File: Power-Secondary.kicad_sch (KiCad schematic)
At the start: 37 parts, among them J1 SUPP PWR MON, J2 SUPP PWR 1, J3 SUPP PWR 2, J4 DCDC SUPPLY, J5 FUSE OUT, J6 SUPP OUT, J7 LV ENABLE, Q1 S1G1D2S2G2D1, Q1A1 IRFU5305PbF, Q1A2 IRFU5305PbF, Q1A3 IRFU5305PbF, Q1A4 IRFU5305PbF, Q2 S1G1D2S2G2D1, Q3 FDD86250-F085

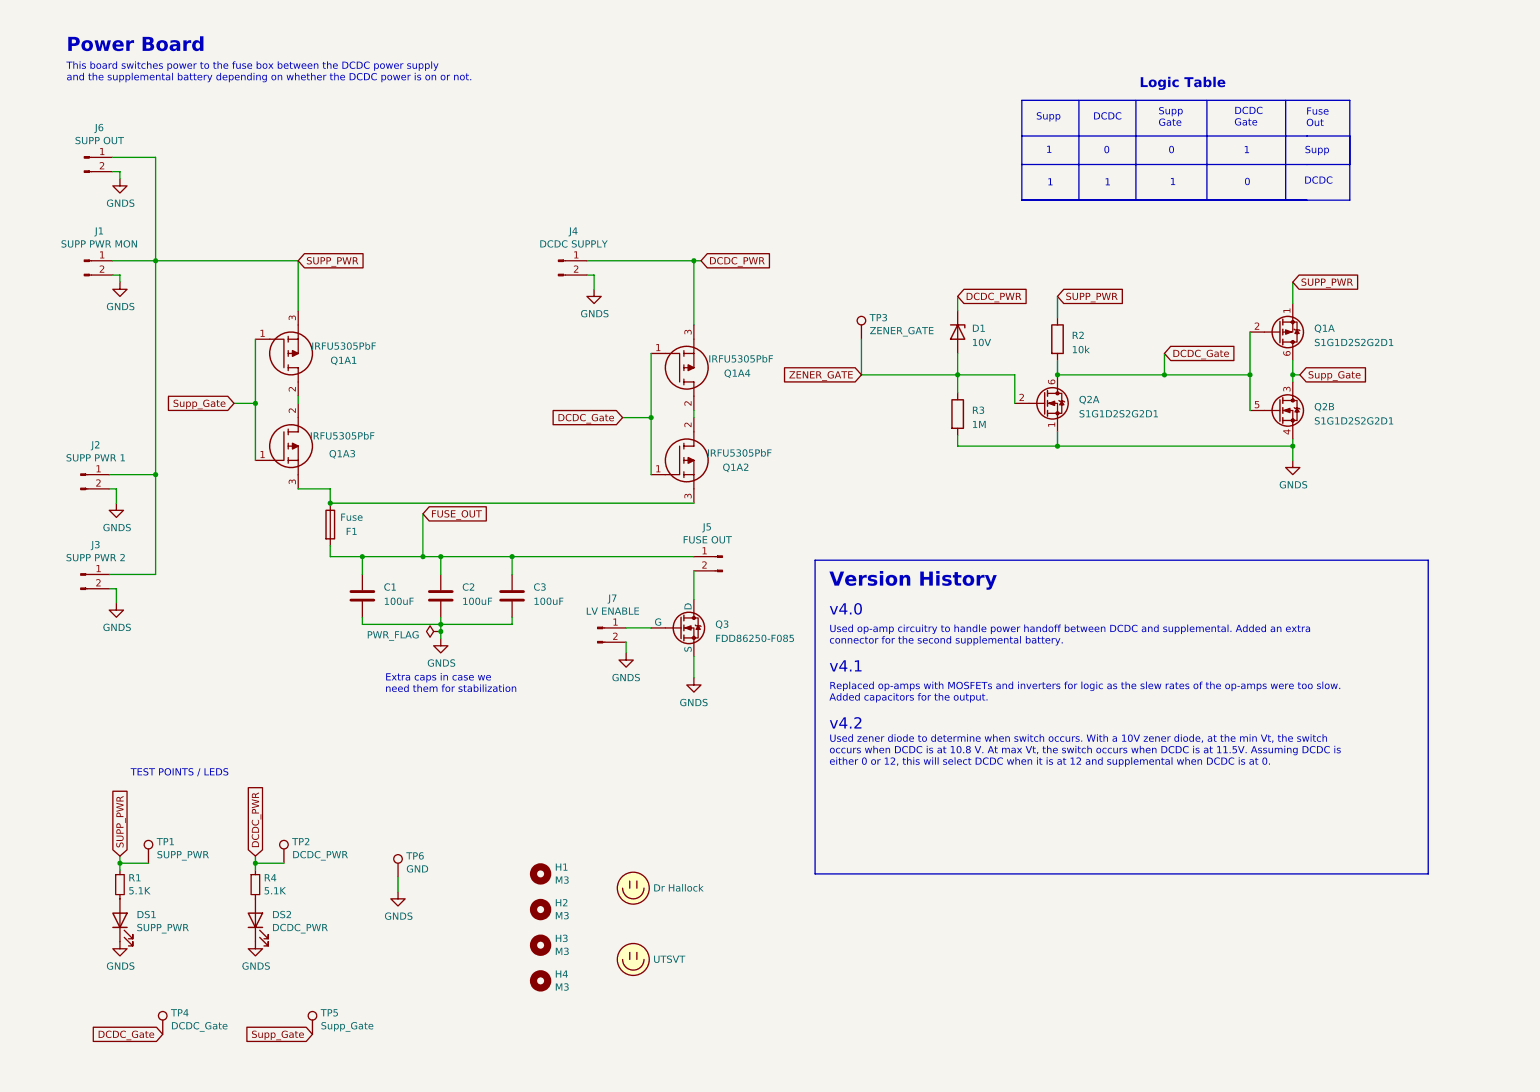
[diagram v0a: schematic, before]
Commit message: Ltc4421 v1.0 (#12)
* LTC4421 Symbol creation

* early sch

* early sch

* changes

* Improved organization of sch

* added circuitry for sch

* Added MOSFET to symbol library

* Finished sch

* footprint assignments

* changes to Power Board sch

* CAD models, symbols update, and footprints

* Pull up and Pull down configs for VALID, DISABLE, SHDN, RETRY

* small changes

* Library fixes and sch changes

* Sch changes

* changes to sch

* assigned footprints

* Excel calculator

* Adjusted resistor divider values and specified more components in the BOM

* Completed BOM for the most part

* sch iteration 1 complete plssssssssss

* final footprint assignments

* initial layout

* added another current sense resistor

* fixed connector pinout

* change SHDN logic

* fixes to sch

* layout complete

* Layout fixes

* made all planes solid filled

* added supp mon connection

* constraint fixes

---------

Co-authored-by: choafe <cryn.hoang@gmail.com>
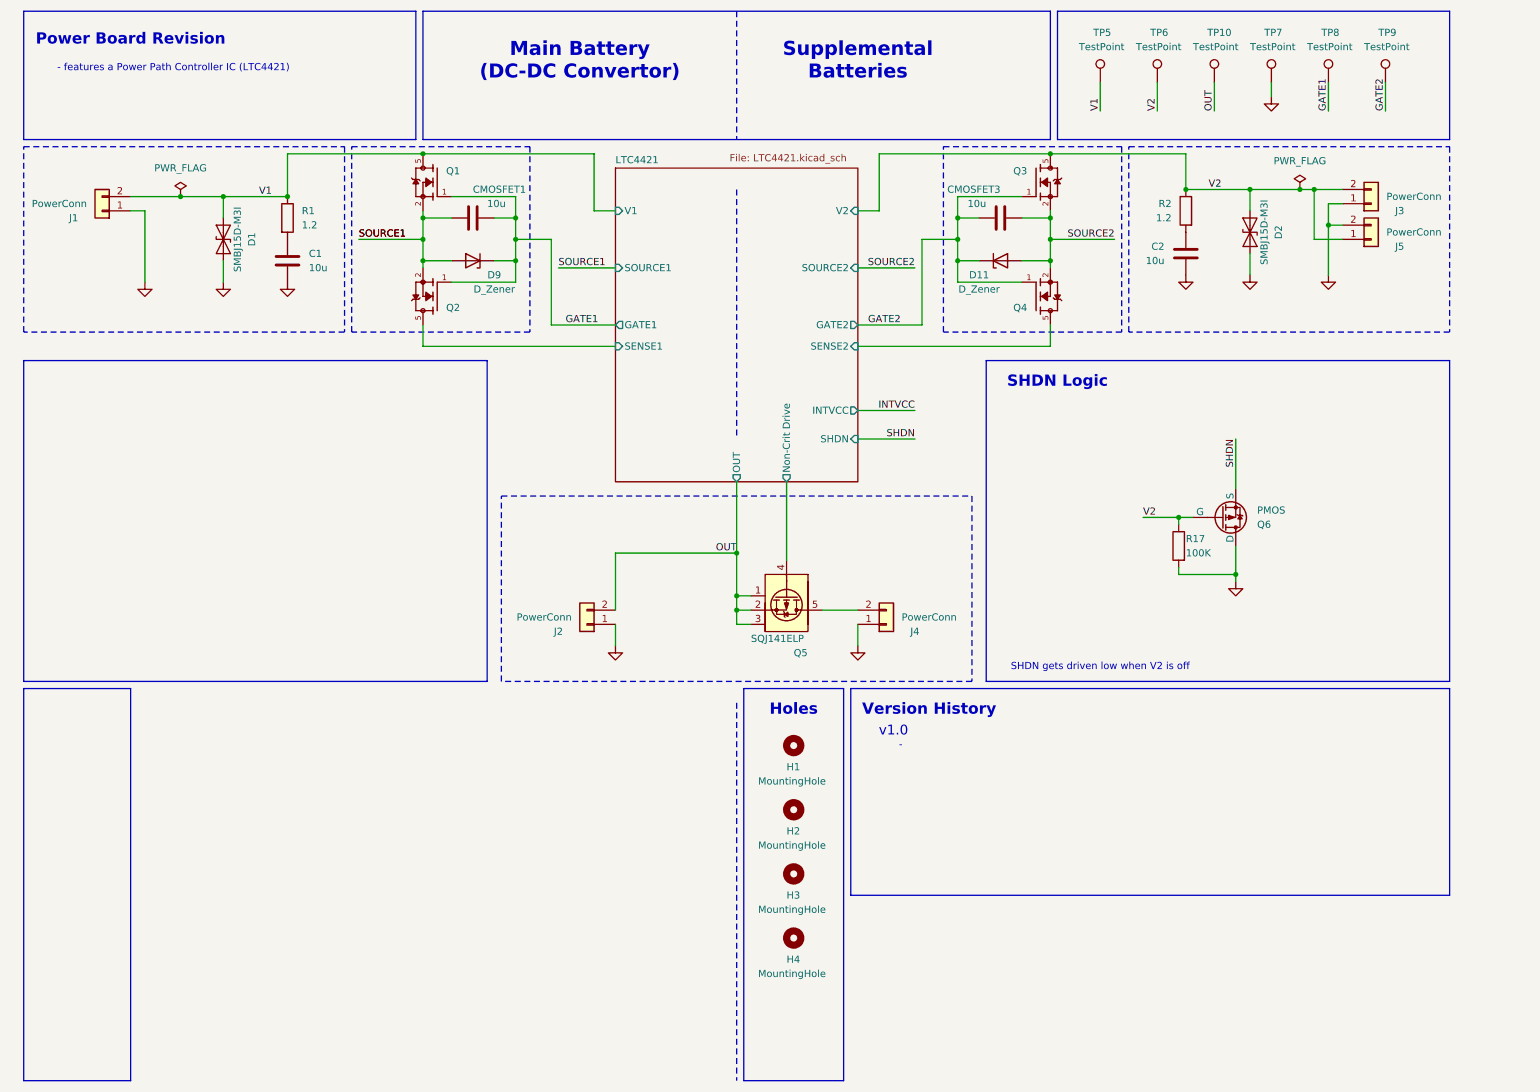
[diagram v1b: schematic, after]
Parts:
- removed C1, C2, C3: 100uF, Capacitor_SMD:C_1210_3225Metric, symbol Device:C
- removed D1: 10V, UTSVT_PowerSupp:SOD2512X110N, symbol Device:D_Zener
- removed DS1: SUPP_PWR, Diode_SMD:D_0805_2012Metric, symbol Device:LED
- removed DS2: DCDC_PWR, Diode_SMD:D_0805_2012Metric, symbol Device:LED
- removed F1: Fuse, Fuse:Fuseholder_Blade_Mini_Keystone_3568, symbol Device:Fuse
- removed J1: SUPP PWR MON, Connector_Molex:Molex_Micro-Fit_3.0_43650-0215_1x02_P3.00mm_Vertical, symbol Connector:Conn_01x02_Pin
- removed J2: SUPP PWR 1, Connector_Molex:Molex_Sabre_43160-0102_1x02_P7.49mm_Vertical, symbol Connector:Conn_01x02_Pin
- removed J3: SUPP PWR 2, Connector_Molex:Molex_Sabre_43160-0102_1x02_P7.49mm_Vertical, symbol Connector:Conn_01x02_Pin
- removed J4: DCDC SUPPLY, Connector_Molex:Molex_Sabre_43160-0102_1x02_P7.49mm_Vertical, symbol Connector:Conn_01x02_Pin
- removed J5: FUSE OUT, Connector_Molex:Molex_Sabre_43160-0102_1x02_P7.49mm_Vertical, symbol Connector:Conn_01x02_Pin
- removed J6: SUPP OUT, Connector_Molex:Molex_Micro-Fit_3.0_43650-0215_1x02_P3.00mm_Vertical, symbol Connector:Conn_01x02_Pin
- removed J7: LV ENABLE, Connector_Molex:Molex_Micro-Fit_3.0_43650-0215_1x02_P3.00mm_Vertical, symbol Connector:Conn_01x02_Pin
- removed LOGO1: Dr Hallock, UTSVT_Special:Hallock_Image_Tiny, symbol utsvt-misc:Logo_Placeholder
- removed LOGO2: UTSVT, UTSVT_Special:UTSVT_Logo_Symbol, symbol utsvt-misc:Logo_Placeholder
- removed Q1: S1G1D2S2G2D1, UTSVT_PowerSupp:SOT65P210X100-6N, symbol Device:Q_Dual_PMOS_S1G1D2S2G2D1
- removed Q1A1, Q1A2, Q1A3, Q1A4: IRFU5305PbF, UTSVT_PowerSupp:SUP90P06-PCHAN-ENH-PWR-MOSFET, symbol utsvt-powersupp:SUP90P06-PCHANNEL-MOSFET
- removed Q2: S1G1D2S2G2D1, UTSVT_PowerSupp:SOT65P210X100-6N, symbol Device:Q_Dual_NMOS_S1G1D2S2G2D1
- removed Q3: FDD86250-F085, UTSVT_PowerSupp:FDD13AN06A0F085, symbol Simulation_SPICE:NMOS
- removed R1, R4: 5.1K, Resistor_SMD:R_0805_2012Metric, symbol Device:R_Small
- removed R3: 1M, Resistor_SMD:R_0603_1608Metric, symbol Device:R
- removed TP1: SUPP_PWR, TestPoint:TestPoint_Pad_2.0x2.0mm, symbol Connector:TestPoint
- removed TP2: DCDC_PWR, TestPoint:TestPoint_Pad_2.0x2.0mm, symbol Connector:TestPoint
- removed TP3: ZENER_GATE, TestPoint:TestPoint_Pad_2.0x2.0mm, symbol Connector:TestPoint
- removed TP4: DCDC_Gate, TestPoint:TestPoint_Pad_2.0x2.0mm, symbol Connector:TestPoint
- added C1, C2, CMOSFET1, CMOSFET3: 10u, Capacitor_SMD:C_0805_2012Metric, symbol ECE319K:C
- added D1, D2: SMBJ15D-M3I, PowerBoardLib:P26_DO-214AA_SMB, symbol PowerBoardLib:SMBJ15D-M3I
- added D11, D9: D_Zener, Diode_SMD:D_SOD-523, symbol Device:D_Zener
- added J1, J2, J3, J4: PowerConn, Connector_Molex:Molex_Sabre_43160-0102_1x02_P7.49mm_Vertical, symbol Connector_Generic:Conn_01x02
- added J5: PowerConn, UTSVT_Connectors:Molex_MicroFit3.0_1x2xP3.00mm_PolarizingPeg_Vertical, symbol Connector_Generic:Conn_01x02
- added Q1, Q2, Q3, Q4: SQJQ140E-T1_GE3, PowerBoardLib:TO200P800X182-5N, symbol PowerBoardLib:SQJQ140E-T1_GE3
- added Q5: SQJ141ELP, Package_SO:PowerPAK_SO-8L_Single, symbol PowerBoardLib:SQJ141ELP
- added Q6: PMOS, Package_TO_SOT_SMD:SOT-23-3, symbol Simulation_SPICE:PMOS
- added R1: 1.2, Resistor_SMD:R_0805_2012Metric, symbol Device:R
- added R17: 100K, Resistor_SMD:R_0805_2012Metric, symbol Device:R
- added TP10, TP7, TP8, TP9: TestPoint, UTSVT_Special:TestPoint_HEX_3mmID, symbol Connector:TestPoint
- H1, H2, H3, H4: value M3 -> MountingHole
- R2: value 10k -> 1.2; footprint Resistor_SMD:R_0603_1608Metric -> Resistor_SMD:R_0805_2012Metric; MFG PN (none) -> RK73H2ATTD1R20F
- TP5: value Supp_Gate -> TestPoint; footprint TestPoint:TestPoint_Pad_2.0x2.0mm -> UTSVT_Special:TestPoint_HEX_3mmID
- TP6: value GND -> TestPoint; footprint TestPoint:TestPoint_Pad_2.0x2.0mm -> UTSVT_Special:TestPoint_HEX_3mmID
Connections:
- net SUPP_PWR is gone; now on net V2: R2.1
- net DCDC_Gate: no longer names the net of R2.2
- net DCDC_Gate: now also C2.1
- net GNDS renamed V2
- net V2: now also D2.1 (K), J3.2 (Pin_2), J5.1 (Pin_1), Q3.5, Q6.2 (G), R17.1
- net Supp_Gate renamed V1
- net V1: now also D1.1 (K), J1.2 (Pin_2), Q1.5, R1.1
- new net: C1.1, R1.2
- new net: J4.2 (Pin_2), Q5.5
- new net GATE1: CMOSFET1.1, D9.1 (K), Q1.1, Q2.1, TP8.1
- new net GATE2: CMOSFET3.1, D11.1 (K), Q3.1, Q4.1, TP9.1
- new net GND: C1.2, C2.2, D1.2 (A), D2.2 (A), J1.1 (Pin_1), J2.1 (Pin_1), J3.1 (Pin_1), J4.1 (Pin_1), J5.2 (Pin_2), Q6.1 (D), R17.2, TP7.1
- new net LTC4421/Non-Crit Drive: Q5.4
- new net LTC4421/SENSE1: Q2.5
- new net LTC4421/SENSE2: Q4.5
- new net OUT: J2.2 (Pin_2), Q5.1, Q5.2, Q5.3, TP10.1
- new net SHDN: Q6.3 (S)
- new net SOURCE1: CMOSFET1.2, D9.2 (A), Q1.2, Q1.3, Q1.4, Q2.2, Q2.3, Q2.4
- new net SOURCE2: CMOSFET3.2, D11.2 (A), Q3.2, Q3.3, Q3.4, Q4.2, Q4.3, Q4.4
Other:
- added sheet LTC4421 (LTC4421.kicad_sch)
- note added: "-"
- note added: "- features a Power Path Controller IC (LTC4421)"
- note added: "Holes"
- note added: "Main Battery (DC-DC Convertor)"
- note added: "Power Board Revision"
- note added: "SHDN Logic"
- note added: "SHDN gets driven low when V2 is off"
- note added: "Supplemental Batteries"
- note added: "v1.0"
- note removed: "0"
- note removed: "1"
- note removed: "DCDC"
- note removed: "DCDC Gate"
- note removed: "Extra caps in case we need them for stabilization"
- note removed: "Fuse Out"
- note removed: "Logic Table"
- note removed: "Power Board"
- note removed: "Replaced op-amps with MOSFETs and inverters for logic as the slew rates of the op-amps were too slow. Added capacitors for the output."
- note removed: "Supp"
- note removed: "Supp Gate"
- note removed: "TEST POINTS / LEDS"
- note removed: "This board switches power to the fuse box between the DCDC power supply and the supplemental battery depending on whether the DCDC power is on or not."
- note removed: "Used op-amp circuitry to handle power handoff between DCDC and supplemental. Added an extra connector for the second supplemental battery."
- note removed: "Used zener diode to determine when switch occurs. With a 10V zener diode, at the min Vt, the switch occurs when DCDC is at 10.8 V. At max Vt, the switch occurs when DCDC is at 11.5V. Assuming DCDC is either 0 or 12, this will select DCDC when it is at 12 and supplemental when DCDC is at 0."
- note removed: "v4.0"
- note removed: "v4.1"
- note removed: "v4.2"

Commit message: fixes for IGN and non-crit
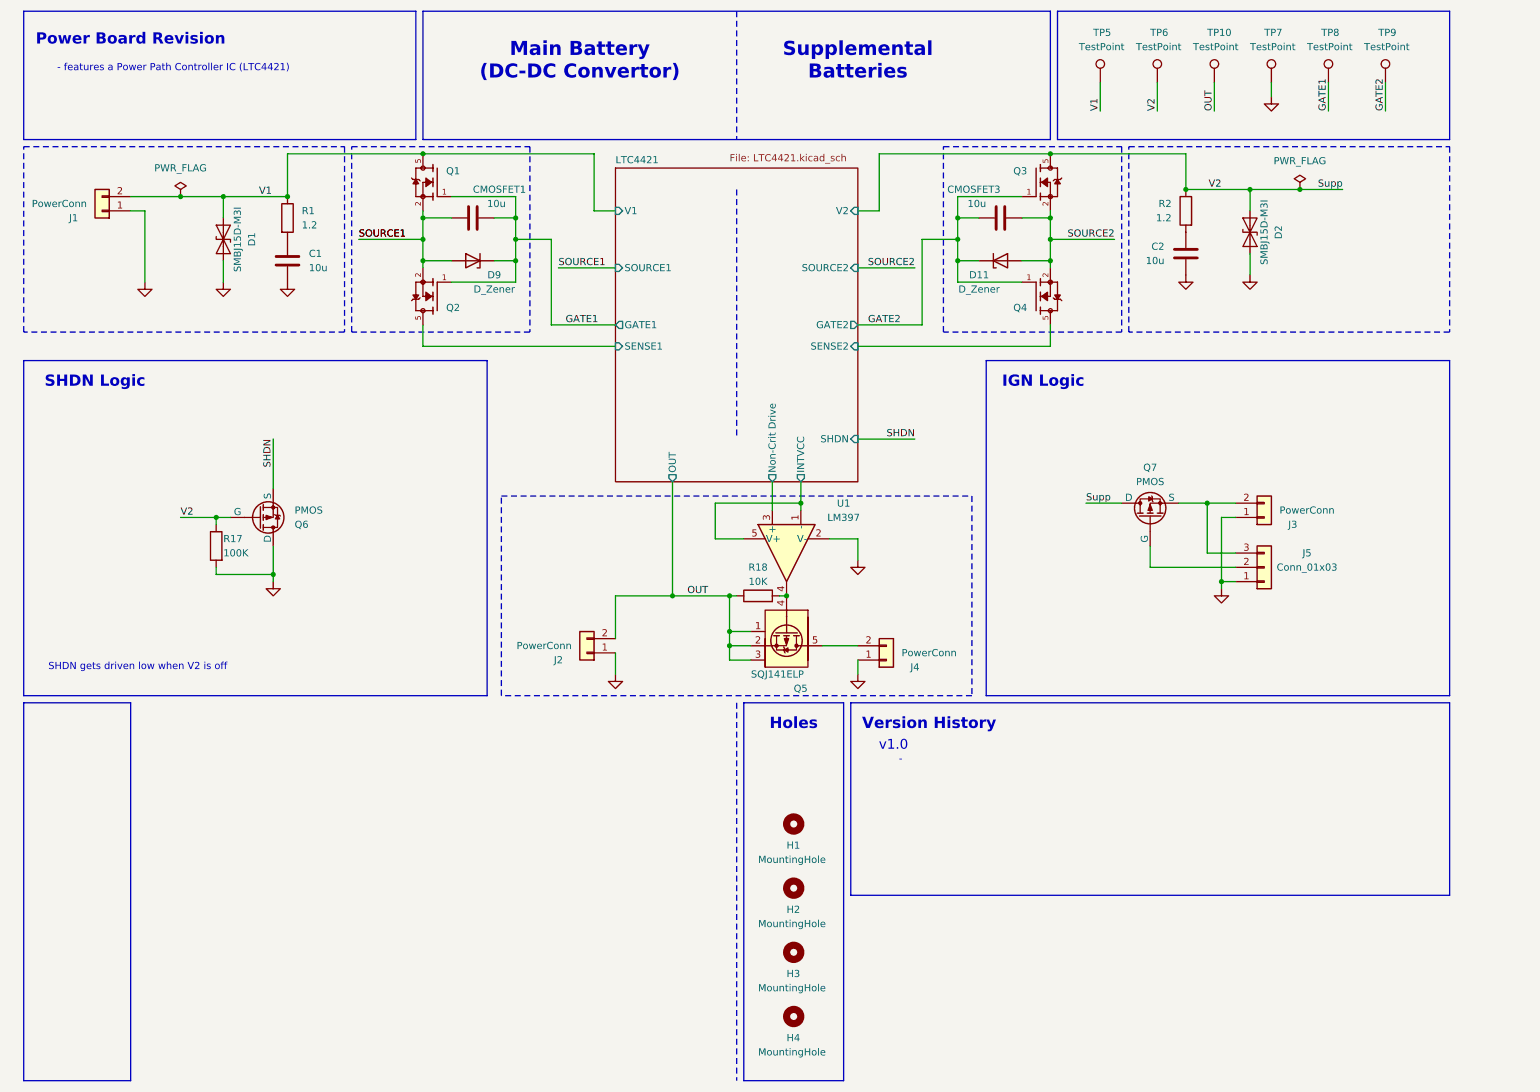
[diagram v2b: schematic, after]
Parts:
- removed J5: PowerConn, UTSVT_Connectors:Molex_MicroFit3.0_1x2xP3.00mm_PolarizingPeg_Vertical, symbol Connector_Generic:Conn_01x02
- added J5: Conn_01x03, symbol Connector_Generic:Conn_01x03
- added Q7: PMOS, symbol Simulation_SPICE:PMOS
- added R18: 10K, Resistor_SMD:R_0805_2012Metric, symbol Device:R
- added U1: LM397, Package_TO_SOT_SMD:SOT-23-5, symbol Comparator:LM397
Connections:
- net GND: now also J5.1 (Pin_1), U1.2 (V-)
- net LTC4421/Non-Crit Drive: now also U1.3 (+); no longer Q5.4
- net OUT: now also R18.1
- net V2 renamed Supp
- net Supp: now also Q7.1 (D); no longer J3.2 (Pin_2)
- new net: Q5.4, R18.2, U1.4
- new net: J5.2 (Pin_2), Q7.2 (G)
- new net: J3.2 (Pin_2), J5.3 (Pin_3), Q7.3 (S)
- new net LTC4421/INTVCC: U1.1 (-), U1.5 (V+)
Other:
- note added: "IGN Logic"
- moved on the sheet: H1, H2, H3, H4, J2, J4, Q5, Q6, R17

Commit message: SHDN, non-crit, and ignition sequence fixes
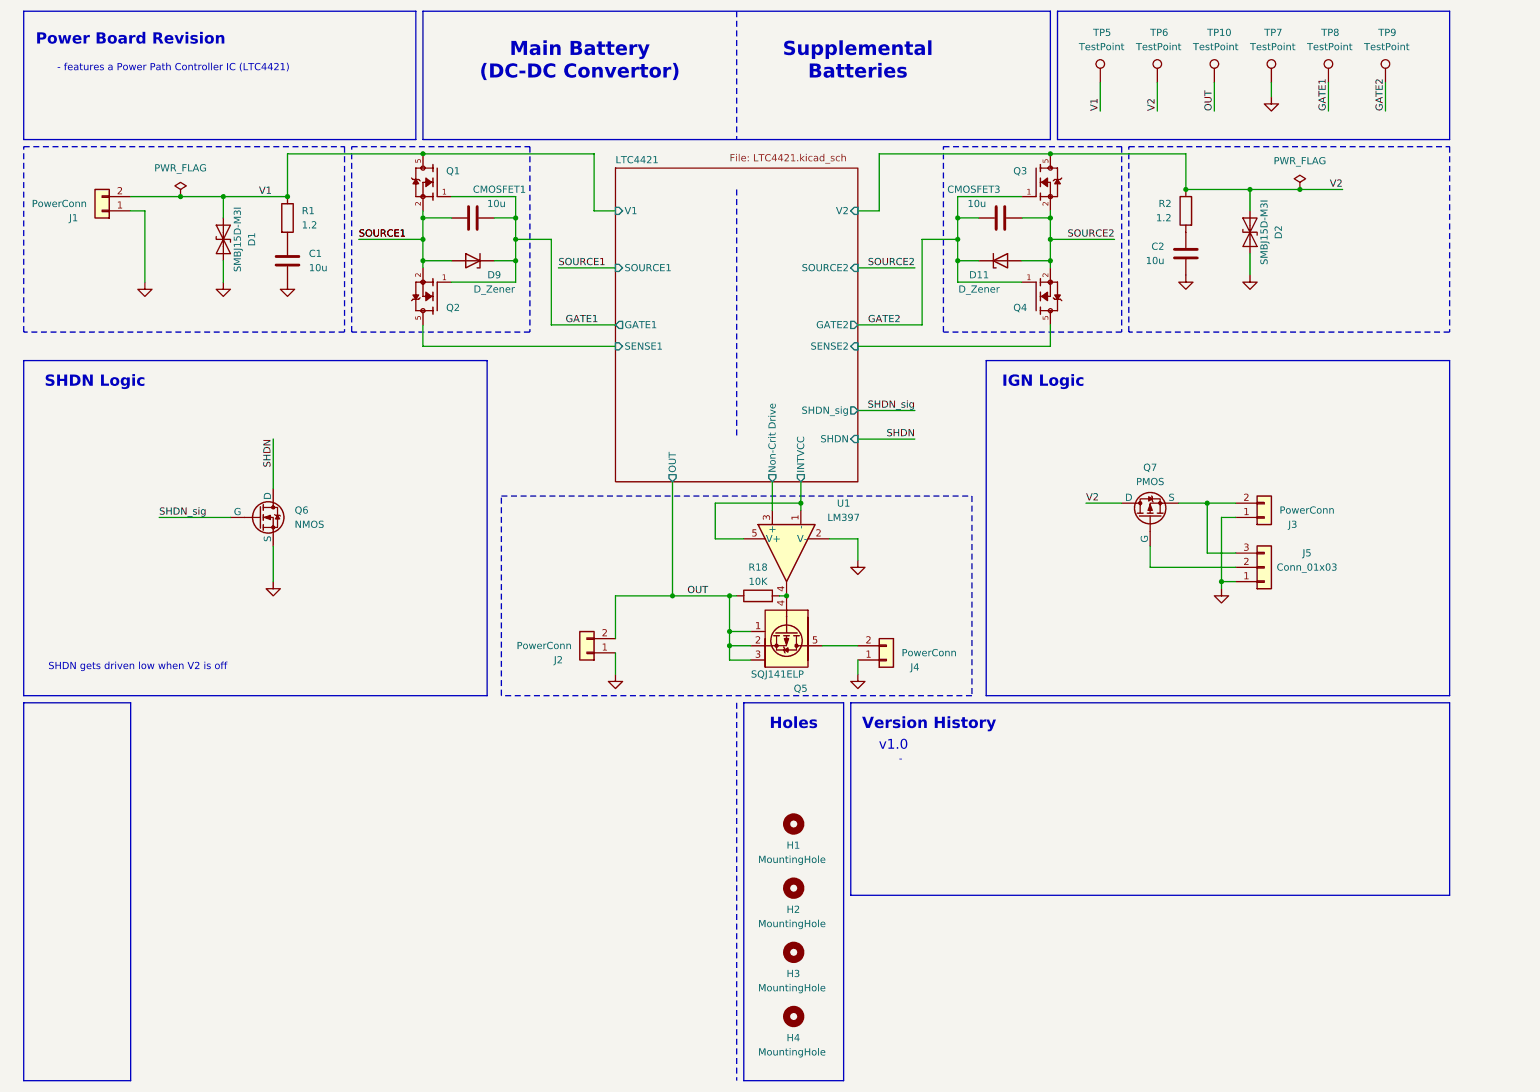
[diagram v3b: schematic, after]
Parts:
- removed Q6: PMOS, Package_TO_SOT_SMD:SOT-23-3, symbol Simulation_SPICE:PMOS
- removed R17: 100K, Resistor_SMD:R_0805_2012Metric, symbol Device:R
- added Q6: NMOS, Package_TO_SOT_SMD:SOT-23, symbol Simulation_SPICE:NMOS
- J5: footprint (none) -> Connector_Molex:Molex_Micro-Fit_3.0_43650-0315_1x03_P3.00mm_Vertical
- Q7: footprint (none) -> Package_SO:PowerPAK_SO-8_Single
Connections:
- net GND: now also Q6.3 (S)
- net SHDN: now also Q6.1 (D)
- net Supp renamed V2
- new net SHDN_sig: Q6.2 (G)
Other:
- sheet LTC4421 ports: added SHDN_sig; removed none

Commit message: bruh changes
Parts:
- Q6: footprint Package_TO_SOT_SMD:SOT-23 -> Package_TO_SOT_SMD:TSOT-23
- U1: footprint Package_TO_SOT_SMD:SOT-23-5 -> Package_TO_SOT_SMD:SOT-353_SC-70-5

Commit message: more bruh changes
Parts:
- U1: value LM397 -> TLV9061QDCKRQ1
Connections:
- net LTC4421/INTVCC: now also U1.3 (-); no longer U1.1 (-)
- net LTC4421/Non-Crit Drive: now also U1.1 (+); no longer U1.3 (+)
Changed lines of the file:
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@@
 			)
 		)
-		(property "Value" "LM397"
+		(property "Value" "TLV9061QDCKRQ1"
 			(at 158.75 102.9014 90)
 			(effects
